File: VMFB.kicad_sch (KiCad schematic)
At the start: 137 parts, among them J1 Screw_Terminal_01x02, J10 Conn_01x03_Pin, J11 Conn_01x08_Pin, J12 Conn_01x06_Pin, J13 Conn_01x03_Pin, J14 Conn_01x03_Pin, J15 Conn_01x03_Pin, J16 Conn_01x03_Pin, J17 Conn_01x03_Pin, J18 Conn_01x03_Pin, J19 Conn_01x02_Pin, J2 USB_A_Stacked, J20 Conn_01x03_Pin, J21 Conn_01x02_Pin, J3 USB_B, J4 Barrel_Jack_Switch, J5 Conn_01x02_Pin, J6 Conn_01x03_Pin, J7 Conn_01x02_Pin, J8 Conn_01x03_Pin, J9 Conn_01x03_Pin, Q1 BC547B, Q2 TIP41C, Q3 BC547B, Q4 BC547B, Q5 BD139, Q6 BC547B, Q7 BC547B, Q8 BC547, U1 NE555P, U2 NE555P, U3 LM358, U4 NE555P, U5 NE555P

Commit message: schemati and pcb tweaking
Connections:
- net GND: no longer J18.2 (Pin_2)
- net IR GND: now also J18.2 (Pin_2)
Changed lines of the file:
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@@
     )
   )
-  (global_label "GND" (shape input) (at 137.16 181.61 0) (fields_autoplaced)
+  (global_label "IR GND" (shape input) (at 137.16 181.61 0) (fields_autoplaced)
     (effects (font (size 1.27 1.27)) (justify left))
-    (property "Intersheetrefs" "${INTERSHEET_REFS}" (at 143.9363 181.61 0) (show_name)
+    (property "Intersheetrefs" "${INTERSHEET_REFS}" (at 146.7787 181.61 0) (show_name)
       (effects (font (size 1.27 1.27)) (justify left) hide)
     )

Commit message: schemati and pcb tweaking
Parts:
- renumbered J7 to J6, J6 to J7, Q2 to Q1, Q1 to Q2, R11 to R10, R9 to R11, R25 to R23, R23 to R25, R30 to R29, R29 to R30, R33 to R32, R32 to R33, R5 to R4, R4 to R5, R7 to R6, R6 to R7, R10 to R8, R8 to R9
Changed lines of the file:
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@@
   (symbol (lib_id "Device:R") (at 127 105.41 0) (mirror y) (unit 1)
     (in_bom yes) (on_board yes) (dnp no)
-    (property "Reference" "R11" (at 124.46 106.68 90)
+    (property "Reference" "R10" (at 124.46 106.68 90)
       (effects (font (size 1.27 1.27)) (justify left))
     )
@@
       (project "VMFB"
         (path "/840789ee-60d4-4003-8113-c1b030a45492"
-          (reference "R11") (unit 1)
+          (reference "R10") (unit 1)
         )
       )
@@
   (symbol (lib_id "Device:R") (at 125.73 26.67 180) (unit 1)
     (in_bom yes) (on_board yes) (dnp no)
-    (property "Reference" "R29" (at 123.5181 24.9169 90)
+    (property "Reference" "R30" (at 123.5181 24.9169 90)
       (effects (font (size 1.27 1.27)) (justify left))
     )
@@
       (project "VMFB"
         (path "/840789ee-60d4-4003-8113-c1b030a45492"
-          (reference "R29") (unit 1)
+          (reference "R30") (unit 1)
         )
       )
@@
   (symbol (lib_id "Device:R") (at 156.21 115.57 90) (mirror x) (unit 1)
     (in_bom yes) (on_board yes) (dnp no)
-    (property "Reference" "R8" (at 156.21 118.11 90)
+    (property "Reference" "R9" (at 156.21 118.11 90)
       (effects (font (size 1.27 1.27)))
     )
@@
       (project "VMFB"
         (path "/840789ee-60d4-4003-8113-c1b030a45492"
-          (reference "R8") (unit 1)
+          (reference "R9") (unit 1)
         )
       )
@@
   (symbol (lib_id "Transistor_BJT:BC547") (at 22.86 132.08 0) (unit 1)
     (in_bom yes) (on_board yes) (dnp no)
-    (property "Reference" "Q1" (at 27.94 135.89 90)
+    (property "Reference" "Q2" (at 27.94 135.89 90)
       (effects (font (size 1.27 1.27)) (justify left))
     )
@@
       (project "VMFB"
         (path "/840789ee-60d4-4003-8113-c1b030a45492"
-          (reference "Q1") (unit 1)
+          (reference "Q2") (unit 1)
         )
       )
@@
   (symbol (lib_id "Device:R") (at 92.71 120.65 0) (mirror y) (unit 1)
     (in_bom yes) (on_board yes) (dnp no)
-    (property "Reference" "R6" (at 95.25 119.38 90)
+    (property "Reference" "R7" (at 95.25 119.38 90)
       (effects (font (size 1.27 1.27)) (justify right))
     )
@@
       (project "VMFB"
         (path "/840789ee-60d4-4003-8113-c1b030a45492"
-          (reference "R6") (unit 1)
+          (reference "R7") (unit 1)
         )
       )
@@
   (symbol (lib_id "Device:R") (at 39.37 60.96 270) (mirror x) (unit 1)
     (in_bom yes) (on_board yes) (dnp no)
-    (property "Reference" "R32" (at 36.83 62.23 90)
+    (property "Reference" "R33" (at 36.83 62.23 90)
       (effects (font (size 1.27 1.27)) (justify right))
     )
@@
       (project "VMFB"
         (path "/840789ee-60d4-4003-8113-c1b030a45492"
-          (reference "R32") (unit 1)
+          (reference "R33") (unit 1)
         )
       )
@@
   (symbol (lib_id "Device:R") (at 87.63 120.65 0) (mirror y) (unit 1)
     (in_bom yes) (on_board yes) (dnp no)
-    (property "Reference" "R9" (at 90.17 119.38 90)
+    (property "Reference" "R11" (at 90.17 119.38 90)
       (effects (font (size 1.27 1.27)) (justify right))
     )
@@
       (project "VMFB"
         (path "/840789ee-60d4-4003-8113-c1b030a45492"
-          (reference "R9") (unit 1)
+          (reference "R11") (unit 1)
         )
       )
@@
   (symbol (lib_id "Transistor_BJT:TIP41C") (at 162.56 120.65 270) (unit 1)
     (in_bom yes) (on_board yes) (dnp no)
-    (property "Reference" "Q2" (at 159.3487 128.6781 90)
+    (property "Reference" "Q1" (at 159.3487 128.6781 90)
       (effects (font (size 1.27 1.27)) (justify left))
     )
@@
       (project "VMFB"
         (path "/840789ee-60d4-4003-8113-c1b030a45492"
-          (reference "Q2") (unit 1)
+          (reference "Q1") (unit 1)
         )
       )
@@
   (symbol (lib_id "Connector:Conn_01x03_Pin") (at 236.22 147.32 0) (unit 1)
     (in_bom yes) (on_board yes) (dnp no)
-    (property "Reference" "J6" (at 237.49 140.97 0)
+    (property "Reference" "J7" (at 237.49 140.97 0)
       (effects (font (size 1.27 1.27)))
     )
@@
       (project "VMFB"
         (path "/840789ee-60d4-4003-8113-c1b030a45492"
-          (reference "J6") (unit 1)
+          (reference "J7") (unit 1)
         )
       )
@@
   (symbol (lib_id "Device:R") (at 25.4 120.65 0) (mirror y) (unit 1)
     (in_bom yes) (on_board yes) (dnp no)
-    (property "Reference" "R4" (at 23.3514 119.2159 90)
+    (property "Reference" "R5" (at 23.3514 119.2159 90)
       (effects (font (size 1.27 1.27)) (justify right))
     )
@@
       (project "VMFB"
         (path "/840789ee-60d4-4003-8113-c1b030a45492"
-          (reference "R4") (unit 1)
+          (reference "R5") (unit 1)
         )
       )
@@
   (symbol (lib_id "Device:R") (at 157.48 44.45 270) (mirror x) (unit 1)
     (in_bom yes) (on_board yes) (dnp no)
-    (property "Reference" "R30" (at 157.48 41.91 90)
+    (property "Reference" "R29" (at 157.48 41.91 90)
       (effects (font (size 1.27 1.27)))
     )
@@
       (project "VMFB"
         (path "/840789ee-60d4-4003-8113-c1b030a45492"
-          (reference "R30") (unit 1)
+          (reference "R29") (unit 1)
         )
       )
@@
   (symbol (lib_id "Device:R") (at 80.01 38.1 270) (unit 1)
     (in_bom yes) (on_board yes) (dnp no)
-    (property "Reference" "R33" (at 80.01 35.56 90)
+    (property "Reference" "R32" (at 80.01 35.56 90)
       (effects (font (size 1.27 1.27)))
     )
@@
       (project "VMFB"
         (path "/840789ee-60d4-4003-8113-c1b030a45492"
-          (reference "R33") (unit 1)
+          (reference "R32") (unit 1)
         )
       )
@@
   (symbol (lib_id "Device:R") (at 160.02 53.34 270) (unit 1)
     (in_bom yes) (on_board yes) (dnp no)
-    (property "Reference" "R25" (at 160.02 50.8 90)
+    (property "Reference" "R23" (at 160.02 50.8 90)
       (effects (font (size 1.27 1.27)))
     )
@@
       (project "VMFB"
         (path "/840789ee-60d4-4003-8113-c1b030a45492"
-          (reference "R25") (unit 1)
+          (reference "R23") (unit 1)
         )
       )
@@
   (symbol (lib_id "Device:R") (at 162.56 111.76 0) (mirror x) (unit 1)
     (in_bom yes) (on_board yes) (dnp no)
-    (property "Reference" "R7" (at 165.1 110.49 90)
+    (property "Reference" "R6" (at 165.1 110.49 90)
       (effects (font (size 1.27 1.27)) (justify left))
     )
@@
       (project "VMFB"
         (path "/840789ee-60d4-4003-8113-c1b030a45492"
-          (reference "R7") (unit 1)
+          (reference "R6") (unit 1)
         )
       )
@@
   (symbol (lib_id "Device:R") (at 74.93 121.92 270) (unit 1)
     (in_bom yes) (on_board yes) (dnp no)
-    (property "Reference" "R10" (at 74.93 119.38 90)
+    (property "Reference" "R8" (at 74.93 119.38 90)
       (effects (font (size 1.27 1.27)))
     )
@@
       (project "VMFB"
         (path "/840789ee-60d4-4003-8113-c1b030a45492"
-          (reference "R10") (unit 1)
+          (reference "R8") (unit 1)
         )
       )
@@
   (symbol (lib_id "Device:R") (at 127 125.73 0) (mirror x) (unit 1)
     (in_bom yes) (on_board yes) (dnp no)
-    (property "Reference" "R5" (at 124.46 127 90)
+    (property "Reference" "R4" (at 124.46 127 90)
       (effects (font (size 1.27 1.27)) (justify right))
     )
@@
       (project "VMFB"
         (path "/840789ee-60d4-4003-8113-c1b030a45492"
-          (reference "R5") (unit 1)
+          (reference "R4") (unit 1)
         )
       )
@@
   (symbol (lib_id "Connector:Conn_01x02_Pin") (at 167.64 100.33 180) (unit 1)
     (in_bom yes) (on_board yes) (dnp no)
-    (property "Reference" "J7" (at 167.64 95.25 0)
+    (property "Reference" "J6" (at 167.64 95.25 0)
       (effects (font (size 1.27 1.27)))
     )
@@
       (project "VMFB"
         (path "/840789ee-60d4-4003-8113-c1b030a45492"
-          (reference "J7") (unit 1)
+          (reference "J6") (unit 1)
         )
       )
@@
   (symbol (lib_id "Device:R") (at 38.1 76.2 90) (unit 1)
     (in_bom yes) (on_board yes) (dnp no)
-    (property "Reference" "R23" (at 38.735 78.74 0)
+    (property "Reference" "R25" (at 38.735 78.74 0)
       (effects (font (size 1.27 1.27)) (justify right))
     )
@@
       (project "VMFB"
         (path "/840789ee-60d4-4003-8113-c1b030a45492"
-          (reference "R23") (unit 1)
+          (reference "R25") (unit 1)
         )
       )

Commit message: schematic and pcb tweaking
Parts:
- R33: value 47K -> 10K
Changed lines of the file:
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@@
   )
   (wire (pts (xy 31.75 31.75) (xy 38.1 31.75))
-    (stroke (width 0) (type default))
+    (stroke (width 0) (type default) (color 255 255 0 1))
   )
   (wire (pts (xy 226.06 67.31) (xy 237.49 67.31))
@@
   )
   (wire (pts (xy 31.75 29.21) (xy 31.75 31.75))
-    (stroke (width 0) (type default))
+    (stroke (width 0) (type default) (color 255 255 0 1))
   )
   (wire (pts (xy 97.79 96.52) (xy 97.79 116.84))
@@
   (symbol (lib_id "Device:Q_Photo_NPN") (at 271.78 116.84 0) (unit 1)
     (in_bom yes) (on_board yes) (dnp no)
-    (property "Reference" "QP6" (at 274.32 116.84 0)
+    (property "Reference" "QP6" (at 273.05 116.84 0)
       (effects (font (size 1.27 1.27)) (justify left))
     )
@@
       (effects (font (size 1.27 1.27)) (justify right))
     )
-    (property "Value" "47K" (at 41.33 60.9695 90)
+    (property "Value" "10K" (at 41.33 60.9695 90)
       (effects (font (size 1.27 1.27)) (justify right))
     )
@@
   (symbol (lib_id "Device:R_Potentiometer") (at 45.72 76.2 0) (mirror y) (unit 1)
     (in_bom yes) (on_board yes) (dnp no)
-    (property "Reference" "RV6" (at 49.53 76.2 90)
+    (property "Reference" "RV6" (at 48.26 76.2 90)
       (effects (font (size 1.27 1.27)))
     )
-    (property "Value" "100K" (at 52.07 76.2 90)
+    (property "Value" "100K" (at 45.72 76.2 90)
       (effects (font (size 1.27 1.27)))
     )
@@
   (symbol (lib_id "Device:R") (at 40.64 71.12 90) (unit 1)
     (in_bom yes) (on_board yes) (dnp no)
-    (property "Reference" "R24" (at 41.275 73.66 0)
+    (property "Reference" "R24" (at 38.8101 73.3129 90)
       (effects (font (size 1.27 1.27)) (justify right))
     )
-    (property "Value" "10K" (at 38.735 73.66 0)
+    (property "Value" "10K" (at 38.6682 71.2201 90)
       (effects (font (size 1.27 1.27)) (justify right))
     )
@@
   (symbol (lib_id "Transistor_BJT:BC547") (at 49.53 71.12 0) (unit 1)
     (in_bom yes) (on_board yes) (dnp no)
-    (property "Reference" "Q6" (at 54.61 70.485 0)
+    (property "Reference" "Q6" (at 52.07 72.39 90)
       (effects (font (size 1.27 1.27)) (justify left))
     )
-    (property "Value" "BC547B" (at 54.61 73.025 0)
+    (property "Value" "BC547B" (at 54.61 74.93 90)
       (effects (font (size 1.27 1.27)) (justify left))
     )
@@
   (symbol (lib_id "Device:R") (at 38.1 76.2 90) (unit 1)
     (in_bom yes) (on_board yes) (dnp no)
-    (property "Reference" "R25" (at 38.735 78.74 0)
+    (property "Reference" "R25" (at 36.3102 78.6713 90)
       (effects (font (size 1.27 1.27)) (justify right))
     )
-    (property "Value" "470R" (at 36.195 78.74 0)
+    (property "Value" "470R" (at 35.56 76.2 90)
       (effects (font (size 1.27 1.27)) (justify right))
     )

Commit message: removed 10K resistor to ground fromo empty sensor
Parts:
- removed R47: 10K, Resistor_THT:R_Axial_DIN0207_L6.3mm_D2.5mm_P2.54mm_Vertical, symbol Device:R
- renumbered R48 to R47
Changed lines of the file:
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@@
   (junction (at 234.95 105.41) (diameter 0) (color 194 0 0 1)
   )
-  (junction (at 189.23 152.4) (diameter 0) (color 0 0 0 0)
-  )
   (junction (at 217.17 105.41) (diameter 0) (color 194 0 0 1)
   )
@@
   (junction (at 30.48 81.28) (diameter 0) (color 0 0 0 1)
   )
-  (junction (at 194.31 144.78) (diameter 0) (color 0 0 0 0)
-  )
   (junction (at 229.87 17.78) (diameter 0) (color 194 0 0 1)
   )
@@
     (stroke (width 0) (type default) (color 204 0 0 1))
   )
-  (wire (pts (xy 194.31 140.97) (xy 194.31 144.78))
-    (stroke (width 0) (type default))
-  )
   (wire (pts (xy 234.95 105.41) (xy 238.76 105.41))
     (stroke (width 0) (type default) (color 204 0 0 1))
@@
     (stroke (width 0) (type default))
   )
-  (wire (pts (xy 194.31 157.48) (xy 194.31 144.78))
+  (wire (pts (xy 194.31 140.97) (xy 194.31 157.48))
     (stroke (width 0) (type default))
   )
@@
     (stroke (width 0) (type default) (color 0 0 0 1))
   )
-  (wire (pts (xy 189.23 144.78) (xy 194.31 144.78))
-    (stroke (width 0) (type default))
-  )
   (wire (pts (xy 237.49 35.56) (xy 240.03 35.56))
     (stroke (width 0) (type default))
@@
   (symbol (lib_id "Device:R") (at 203.2 138.43 0) (mirror y) (unit 1)
     (in_bom yes) (on_board yes) (dnp no)
-    (property "Reference" "R48" (at 201.2088 139.9786 90)
+    (property "Reference" "R47" (at 201.2088 139.9786 90)
       (effects (font (size 1.27 1.27)) (justify left))
     )
@@
       (project "VMFB"
         (path "/840789ee-60d4-4003-8113-c1b030a45492"
-          (reference "R48") (unit 1)
+          (reference "R47") (unit 1)
         )
       )
@@
         )
       )
-    )
-  )
-  (symbol (lib_id "Device:R") (at 189.23 148.59 180) (unit 1)
-    (in_bom yes) (on_board yes) (dnp no)
-    (property "Reference" "R47" (at 191.5108 146.7083 90)
-      (effects (font (size 1.27 1.27)) (justify left))
-    )
-    (property "Value" "10K" (at 189.2463 146.435 90)
-      (effects (font (size 1.27 1.27)) (justify left))
-    )
-    (property "Footprint" "Resistor_THT:R_Axial_DIN0207_L6.3mm_D2.5mm_P2.54mm_Vertical" (at 191.008 148.59 90)
-      (effects (font (size 1.27 1.27)) hide)
-    )
-    (property "Datasheet" "~" (at 189.23 148.59 0)
-      (effects (font (size 1.27 1.27)) hide)
-    )
-    (pin "1")
-    (pin "2")
-    (instances
-      (project "VMFB"
-        (path "/840789ee-60d4-4003-8113-c1b030a45492"
-          (reference "R47") (unit 1)
-        )
-      )

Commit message: removed transistor/resistor disabline PBKA when IR is on = grounding this along with the IR and signal LEDs instead of using another transistor
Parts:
- removed Q2: BC547B, Package_TO_SOT_THT:TO-92_Inline_Wide, symbol Transistor_BJT:BC547
- removed R3: 10K, Resistor_THT:R_Axial_DIN0207_L6.3mm_D2.5mm_P2.54mm_Vertical, symbol Device:R
- renumbered J7 to J6, J6 to J7, Q3 to Q2, Q4 to Q3, Q5 to Q4, Q6 to Q5, Q7 to Q6, Q8 to Q7, R12 to R11, R13 to R12, R14 to R13, R15 to R14, R16 to R15, R17 to R16, R18 to R17, R19 to R18, R20 to R19, R21 to R20, R22 to R21, R24 to R22, R25 to R23, R23 to R24, R26 to R25, R27 to R26, R28 to R27, R30 to R28, R5 to R3, R31 to R30, R33 to R31, R34 to R33, R35 to R34, R36 to R35, R37 to R36, R38 to R37, R39 to R38, R40 to R39, R41 to R40, R42 to R41, R43 to R42, R44 to R43, R45 to R44, R46 to R45, R47 to R46, R7 to R5, R8 to R6, R6 to R7, R9 to R8, R11 to R9
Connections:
- net IR GND: now also R3.2, U1.4 (R)
- net at R11.1: now also RV2.2; no longer RV2.3
- net at D2.2 (A), R6.2, U1.7 (DIS): now also RV2.3; no longer R11.2
- net at J8.1 (Pin_1), R3.1, R39.1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: now also R11.2; no longer RV2.2
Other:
- moved on the sheet: R11, RV2

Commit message: added transistor to the PBKA
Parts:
- removed R5: 47R, Resistor_THT:R_Axial_DIN0309_L9.0mm_D3.2mm_P2.54mm_Vertical, symbol Device:R
- added Q2: BC337, Package_TO_SOT_THT:TO-92_Inline_Wide, symbol Transistor_BJT:BC547
- added R11: 10K, Resistor_THT:R_Axial_DIN0207_L6.3mm_D2.5mm_P2.54mm_Vertical, symbol Device:R
- added R4: 2.2K, Resistor_THT:R_Axial_DIN0207_L6.3mm_D2.5mm_P2.54mm_Vertical, symbol Device:R
- R9: value 10K -> 47R; footprint Resistor_THT:R_Axial_DIN0207_L6.3mm_D2.5mm_P2.54mm_Vertical -> Resistor_THT:R_Axial_DIN0309_L9.0mm_D3.2mm_P2.54mm_Vertical
- renumbered J13 to J12, J14 to J13, J12 to J14, Q2 to Q3, Q3 to Q4, Q4 to Q5, Q5 to Q6, Q6 to Q7, Q7 to Q8, R11 to R12, R12 to R13, R13 to R14, R14 to R15, R15 to R16, R16 to R17, R17 to R18, R18 to R19, R19 to R20, R20 to R21, R21 to R22, R22 to R23, R23 to R24, R24 to R25, R25 to R26, R26 to R27, R27 to R28, R28 to R29, R29 to R30, R30 to R31, R31 to R32, R32 to R33, R33 to R34, R34 to R35, R35 to R36, R36 to R37, R37 to R38, R38 to R39, R39 to R40, R40 to R41, R41 to R42, R42 to R43, R43 to R44, R44 to R45, R45 to R46, R46 to R47, R4 to R5
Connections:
- net GND: now also Q2.3 (E); no longer LED1.1 (K)
- net at J8.1 (Pin_1), R12.2, R3.1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: now also R9.2, R11.1
- net at LED1.2 (A): now also R11.2; no longer R9.2
- net at R9.1: now also LED1.1 (K), Q2.1 (C); no longer U1.3 (Q)
- new net: Q2.2 (B), R4.1
- new net: R4.2, U1.3 (Q)

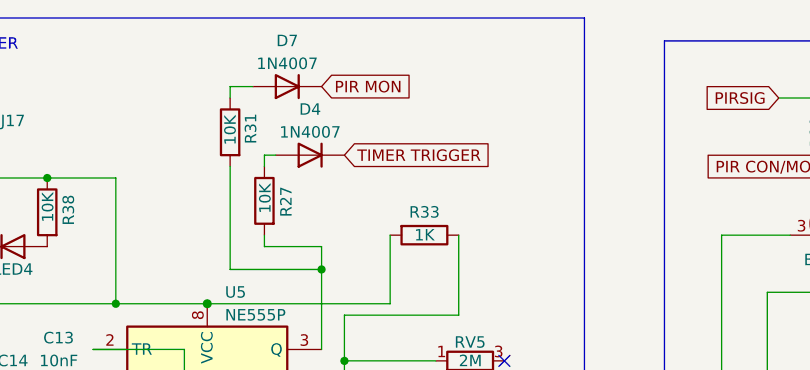
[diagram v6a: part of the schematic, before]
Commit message: fixed timer connection to trigger IR LEDs
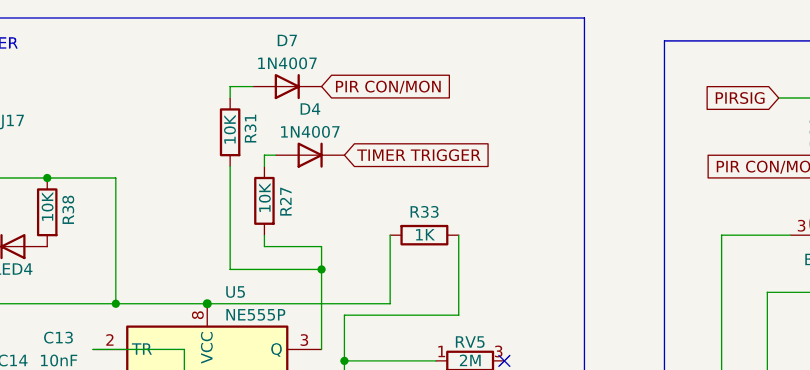
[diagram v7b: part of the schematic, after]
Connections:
- net PIR CON/MON: now also D7.1 (K)
- net PIR MON: no longer D7.1 (K)
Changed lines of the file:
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@@
     )
   )
-  (global_label "PIR MON" (shape input) (at 68.58 21.59 0) (fields_autoplaced)
+  (global_label "PIR CON{slash}MON" (shape input) (at 68.58 21.59 0) (fields_autoplaced)
     (effects (font (size 1.27 1.27)) (justify left))
-    (property "Intersheetrefs" "${INTERSHEET_REFS}" (at 79.7106 21.59 0) (show_name)
+    (property "Intersheetrefs" "${INTERSHEET_REFS}" (at 84.9721 21.59 0) (show_name)
       (effects (font (size 1.27 1.27)) (justify left) hide)
     )
